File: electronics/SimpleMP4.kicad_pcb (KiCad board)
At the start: 2 copper layers, 119 parts, among them J1 USB_OTG, Q1 8050, Q2 SI2305, Q3 SI2305, Q4 8050, Q5 8550, Q6 SI2305, Q7 8550, U1 OCP8020, U2 RK2608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

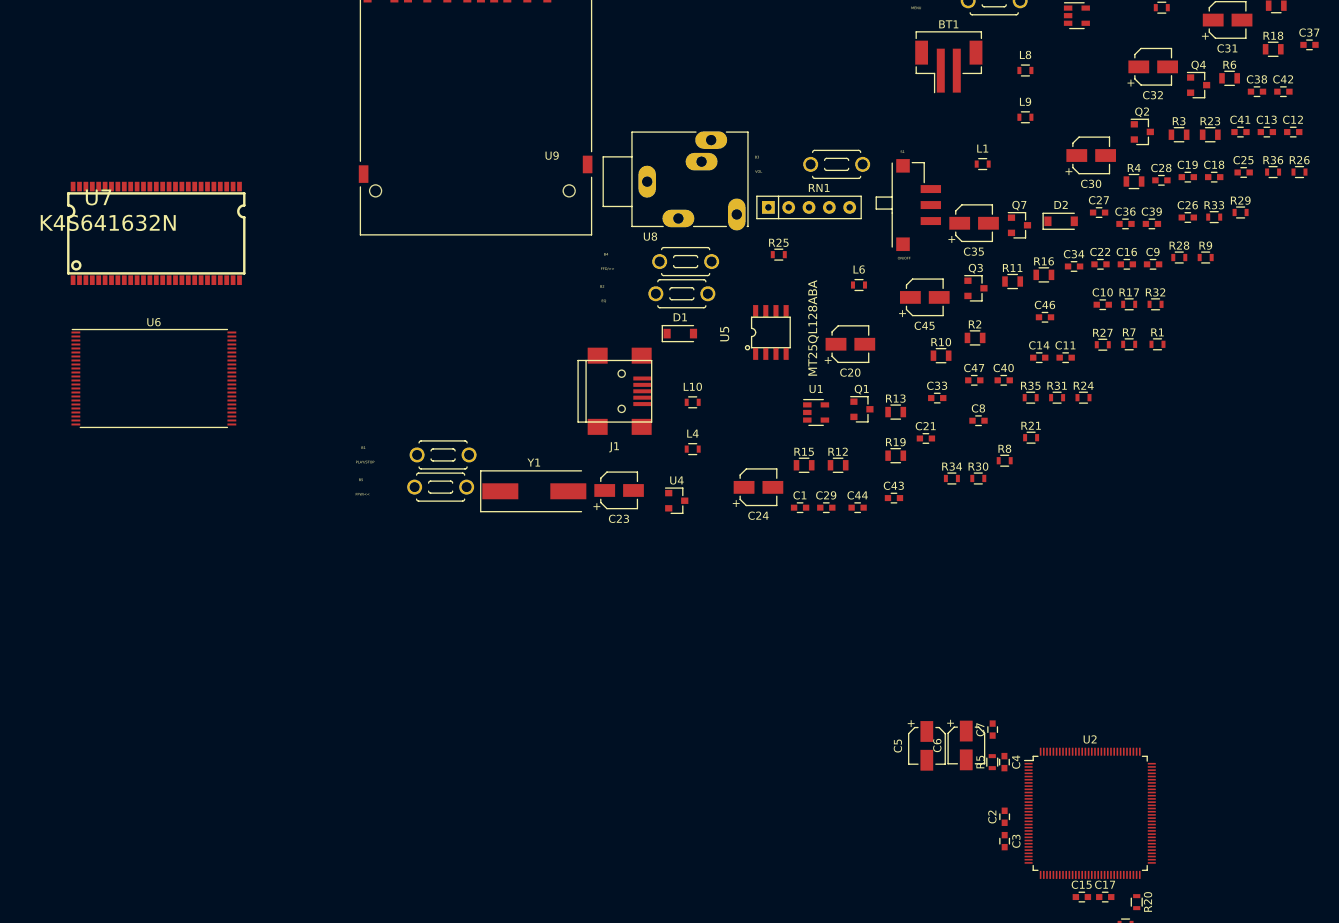
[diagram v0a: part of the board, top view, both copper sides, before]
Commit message: placed most components around rk2608
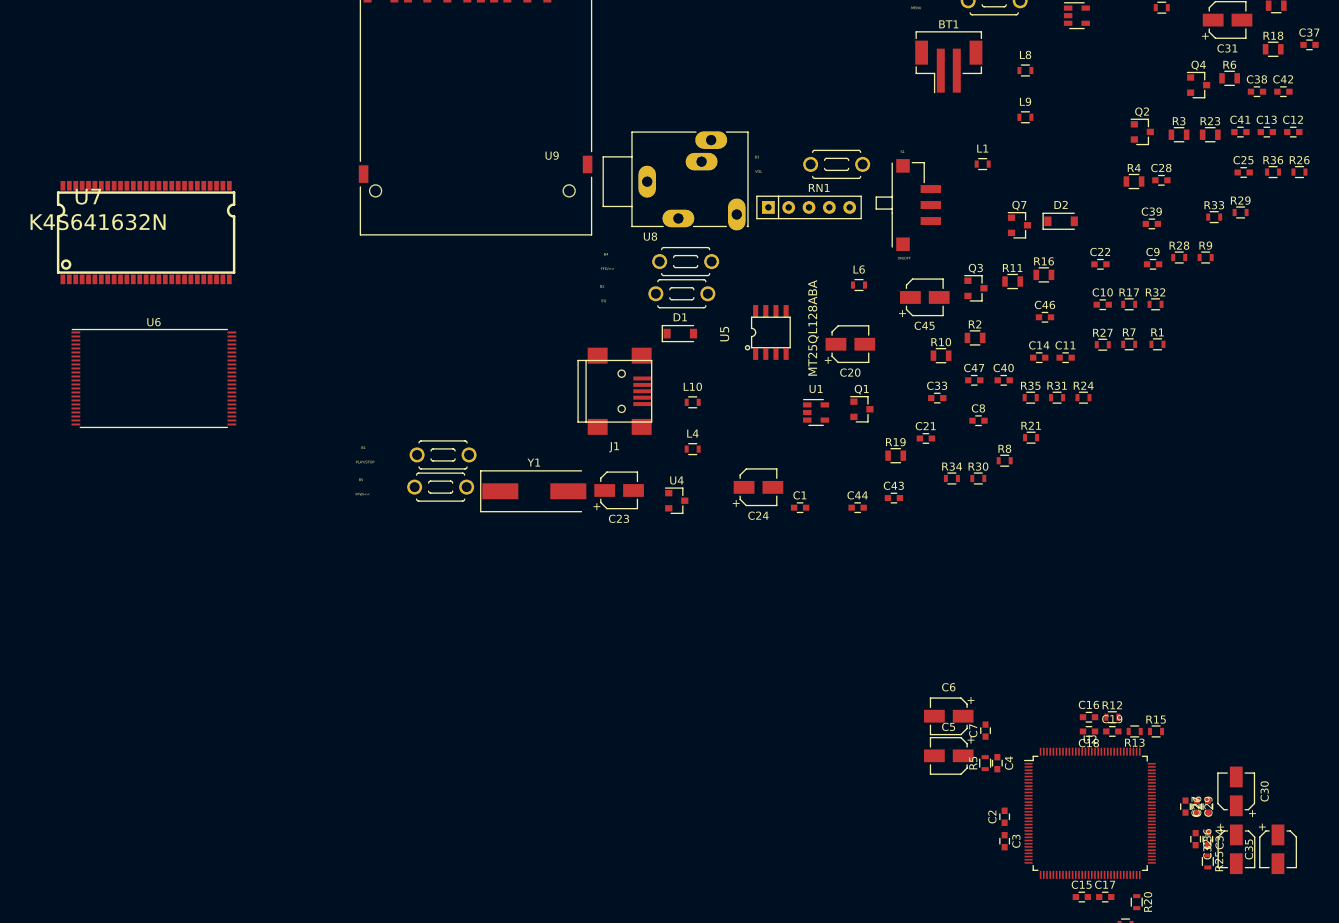
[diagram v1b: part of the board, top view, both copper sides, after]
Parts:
- R12, R13, R15: footprint Resistors_SMD:R_0805 -> Resistors_SMD:R_0603
- moved C32 98.4 mm to (192.2, 133.0), turned to 270 degrees
- moved R25 92.9 mm to (188.6, 134.5), turned to 270 degrees
- moved C35 87.0 mm to (197.4, 133.0), turned to 270 degrees
- moved C30 81.5 mm to (192.2, 125.7), turned to 90 degrees
- moved C36 77.4 mm to (187.1, 131.7), turned to 270 degrees
- moved C27 75.5 mm to (188.6, 127.6), turned to 90 degrees
- moved C26 73.6 mm to (185.8, 127.6), turned to 270 degrees
- moved C34 73.5 mm to (188.6, 131.7), turned to 270 degrees
- moved C18 71.0 mm to (173.7, 118.2), turned to 180 degrees
- moved C19 69.9 mm to (176.7, 118.2)
- moved C29 59.5 mm to (187.2, 127.6), turned to 270 degrees
- moved C16 56.8 mm to (173.7, 116.5)
- moved R15 55.2 mm to (182.1, 118.2)
- moved R13 49.9 mm to (179.5, 118.2), turned to 180 degrees
- moved R12 46.6 mm to (176.7, 116.5)
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
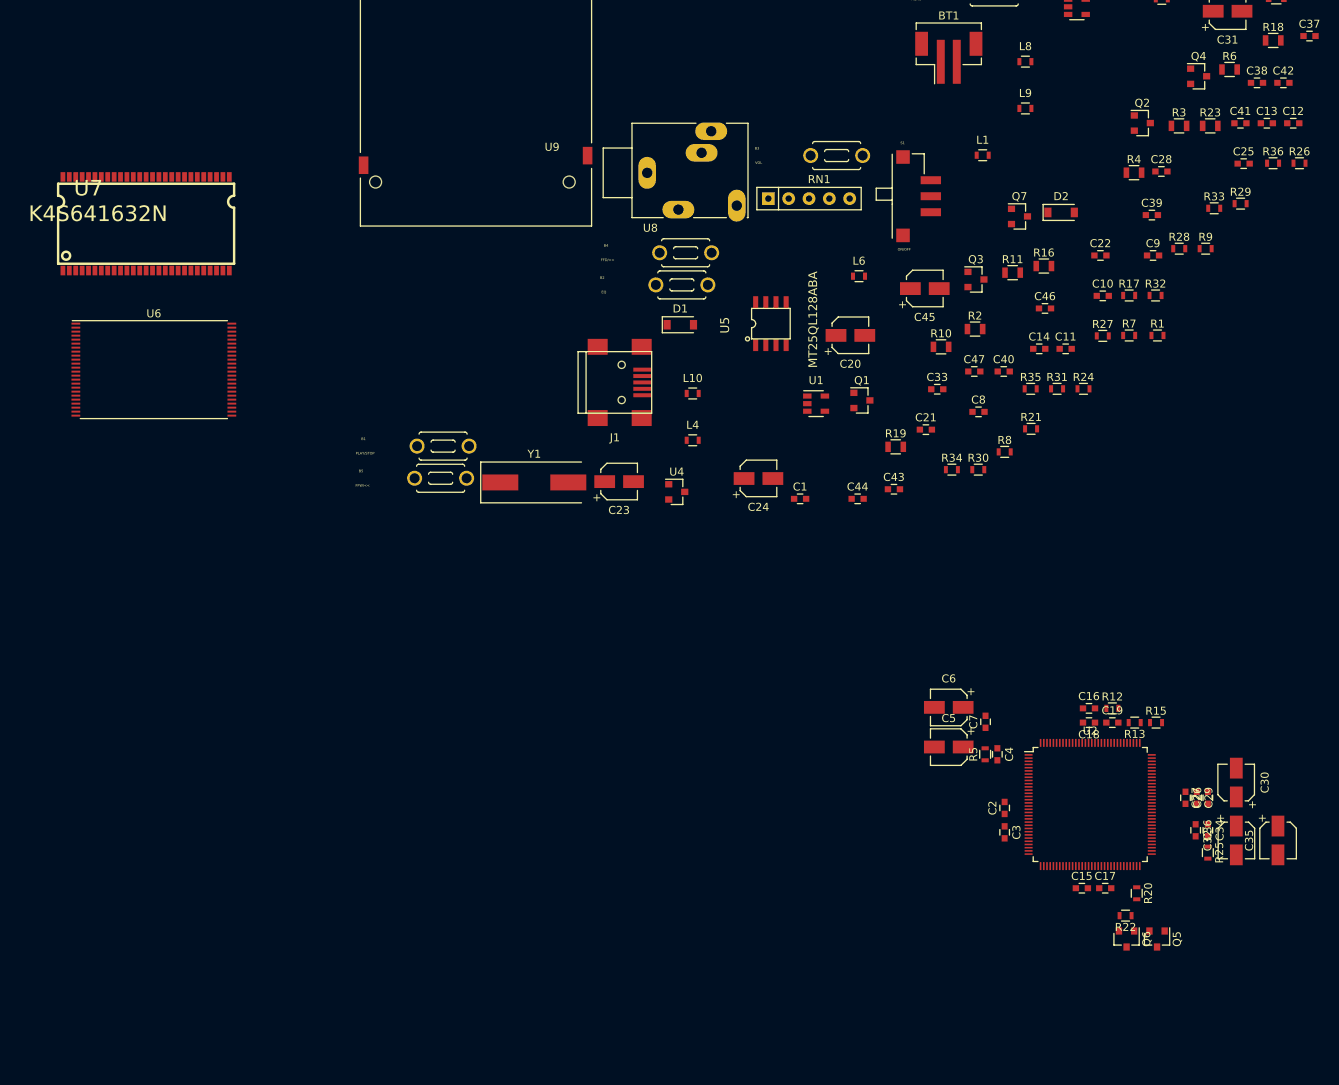
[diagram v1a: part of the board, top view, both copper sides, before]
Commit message: placed USB section
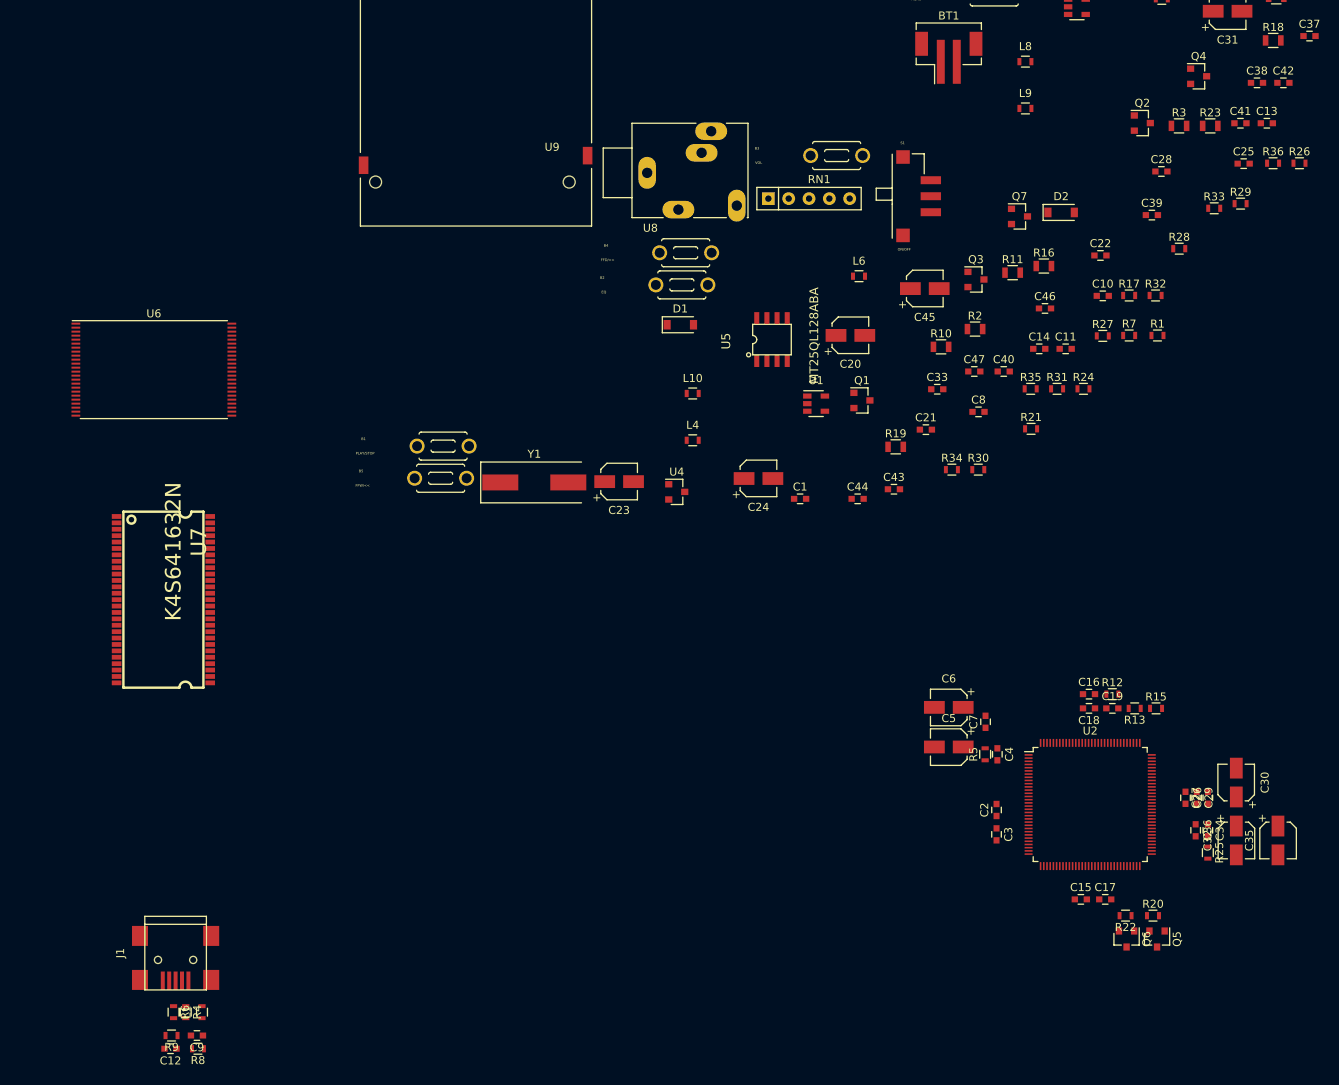
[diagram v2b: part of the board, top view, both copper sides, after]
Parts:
- R4, R6: footprint Resistors_SMD:R_0805 -> Resistors_SMD:R_0603
- moved C12 181.9 mm to (58.9, 159.0), turned to 180 degrees
- moved R6 176.9 mm to (59.3, 154.4), turned to 270 degrees
- moved R9 162.4 mm to (59.1, 157.4), turned to 180 degrees
- moved R4 158.3 mm to (60.8, 154.4), turned to 270 degrees
- moved C9 154.2 mm to (62.2, 157.4), turned to 180 degrees
- moved L1 144.9 mm to (62.9, 154.4), turned to 90 degrees
- moved R8 125.4 mm to (62.4, 159.0), turned to 180 degrees
- moved J1 90.9 mm to (59.6, 147.7), turned to 270 degrees
- moved U7 47.0 mm to (58.0, 102.9), turned to 270 degrees
- moved R20 3.45 mm to (181.7, 142.4), turned to 0 degrees
- moved U5 2.00 mm to (134.1, 70.4)
- moved C16 1.78 mm to (173.7, 114.7)
- moved R12 1.78 mm to (176.7, 114.7)
- moved C18 1.78 mm to (173.7, 116.5)
- moved C19 1.78 mm to (176.7, 116.5)
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
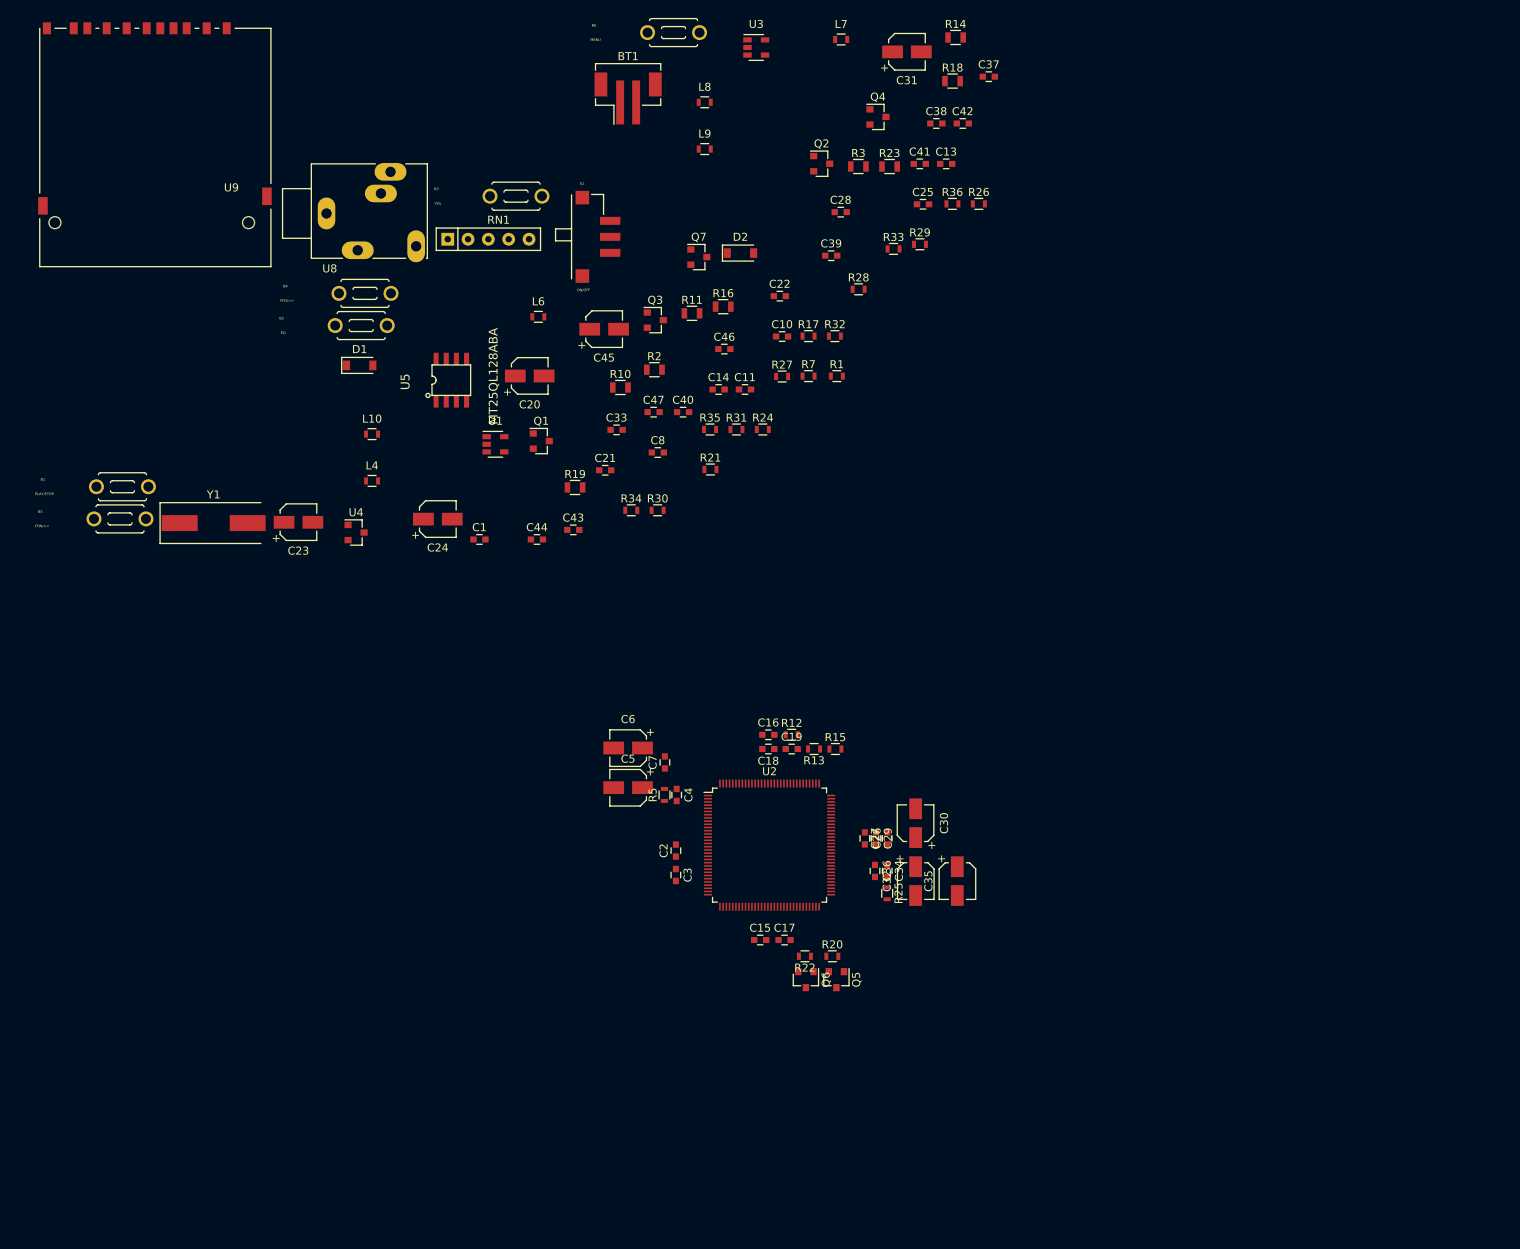
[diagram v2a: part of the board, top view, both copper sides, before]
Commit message: grouped a few more components
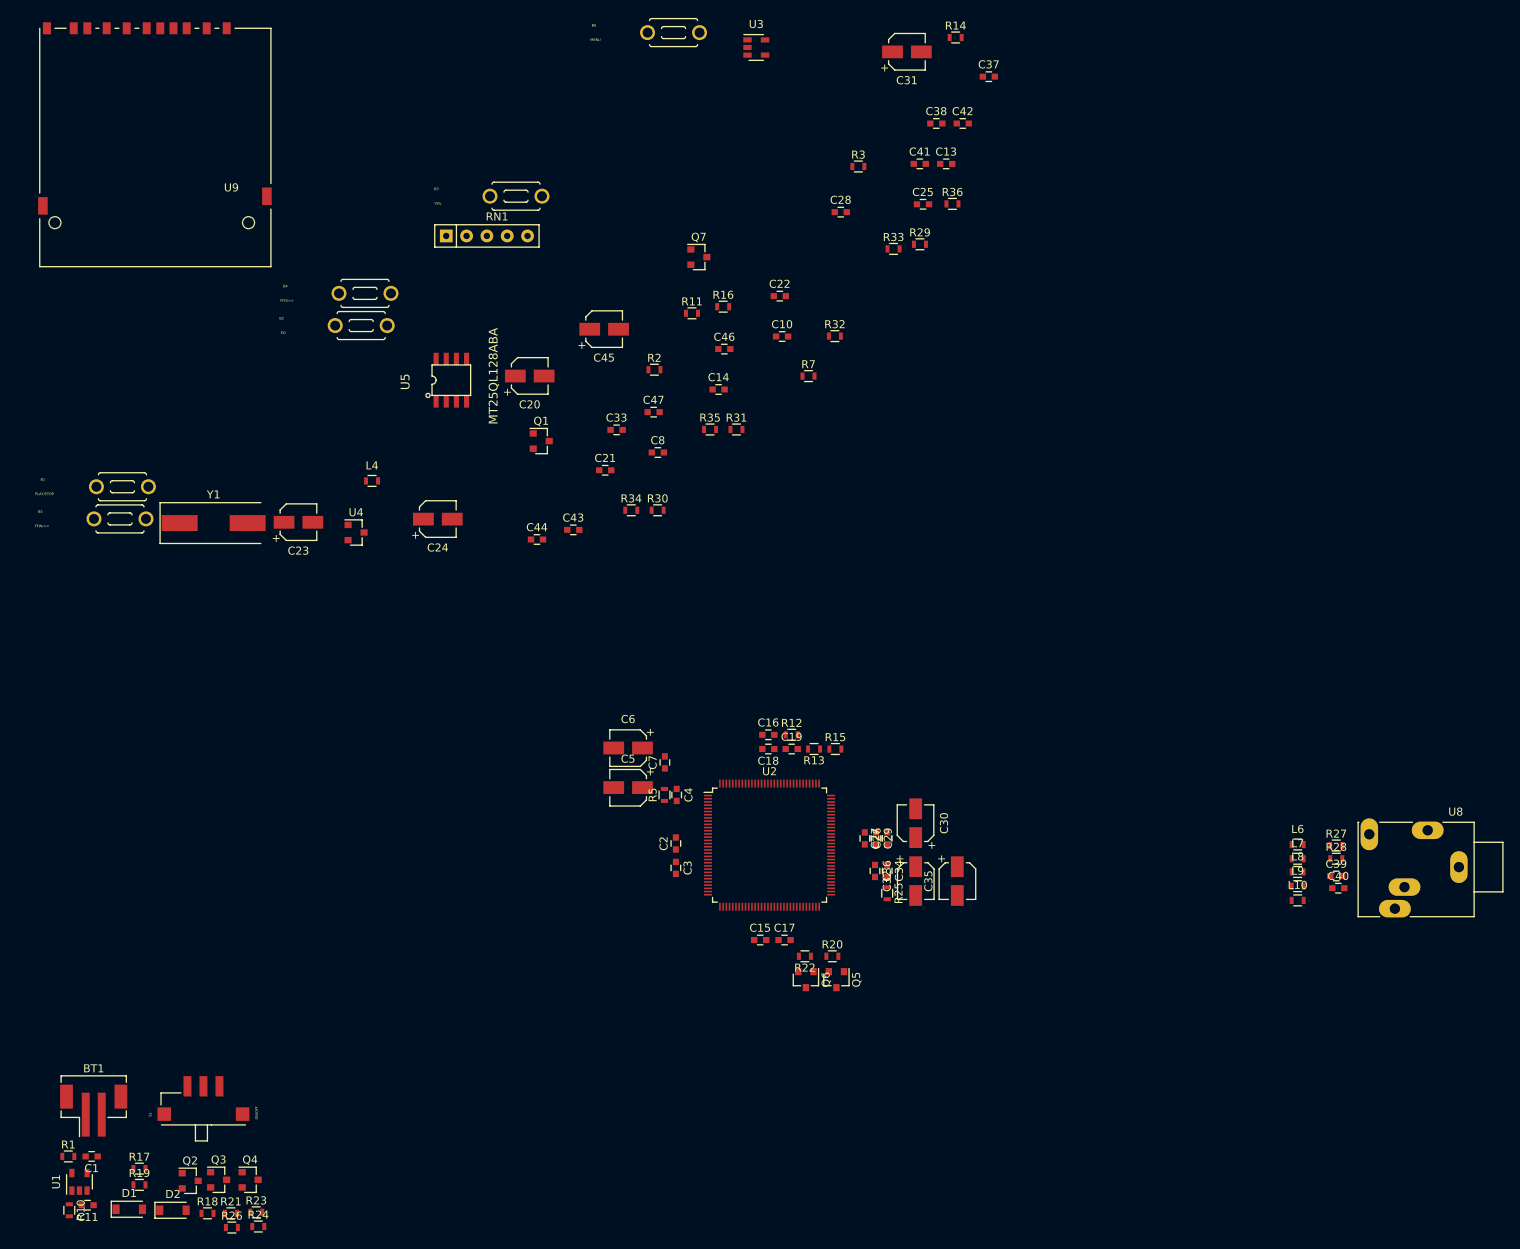
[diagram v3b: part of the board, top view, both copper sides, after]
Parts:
- R10, R11, R14, R16, R18, R19, R2, R23, R3: footprint Resistors_SMD:R_0805 -> Resistors_SMD:R_0603
- moved R18 169.4 mm to (103.6, 174.5)
- moved R26 158.4 mm to (106.7, 176.3)
- moved Q4 154.3 mm to (109.0, 170.3)
- moved R23 152.8 mm to (109.7, 174.4)
- moved U8 152.1 mm to (256.2, 126.6), turned to 180 degrees
- moved Q2 149.6 mm to (101.5, 170.4)
- moved BT1 143.1 mm to (89.4, 161.0)
- moved D2 139.1 mm to (99.3, 174.1)
- moved R1 136.9 mm to (86.2, 167.4)
- moved R17 133.5 mm to (95.1, 168.9)
- moved C11 131.0 mm to (88.6, 173.5), turned to 180 degrees
- moved L10 129.6 mm to (239.9, 135.4)
- moved R10 123.8 mm to (86.4, 174.1), turned to 270 degrees
- moved L8 121.4 mm to (239.9, 131.8)
- moved Q3 120.5 mm to (105.0, 170.3)
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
